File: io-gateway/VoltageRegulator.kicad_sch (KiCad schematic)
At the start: 15 parts, among them U3 TPS54308

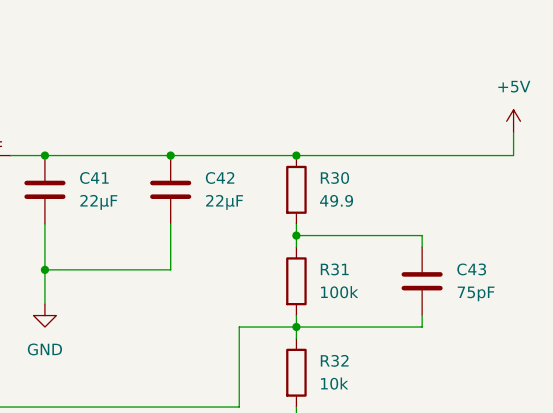
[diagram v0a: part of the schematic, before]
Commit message: increase Pads for Handsolder, fix issue with rectifier
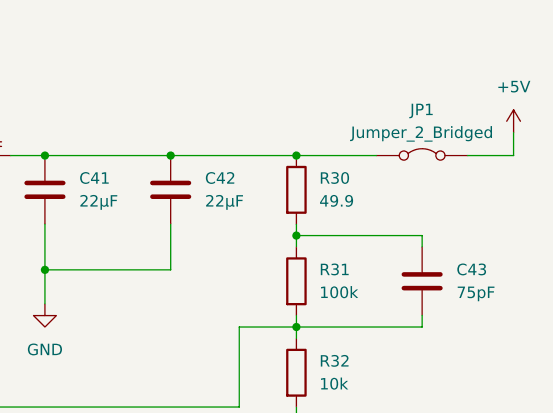
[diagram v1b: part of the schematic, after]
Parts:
- added JP1: Jumper_2_Bridged, Connector_PinHeader_2.54mm:PinHeader_1x02_P2.54mm_Vertical, symbol Jumpers:Jumper_2_Bridged
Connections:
- net +5V: now also JP1.2 (B); no longer C41.1, C42.1, L6.2, R30.1
- new net: C41.1, C42.1, JP1.1 (A), L6.2, R30.1
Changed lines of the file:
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@@
+	)
+	(junction
+		(at 175.26 60.96)
+		(diameter 0)
+		(color 0 0 0 0)
 	)
 	(junction
@@
 	)
 	(junction
-		(at 175.26 60.96)
-		(diameter 0)
-		(color 0 0 0 0)
-	)
-	(junction
 		(at 55.88 58.42)
 		(diameter 0)
@@
 	(wire
 		(pts
+			(xy 175.26 60.96) (xy 184.15 60.96)
+		)
+		(stroke
+			(width 0)
+			(type default)
+		)
+	)
+	(wire
+		(pts
 			(xy 189.23 71.12) (xy 189.23 69.85)
 		)
@@
 	(wire
 		(pts
+			(xy 194.31 60.96) (xy 199.39 60.96)
+		)
+		(stroke
+			(width 0)
+			(type default)
+		)
+	)
+	(wire
+		(pts
 			(xy 175.26 69.85) (xy 175.26 71.12)
 		)
@@
 		(pts
 			(xy 161.29 68.58) (xy 161.29 73.66)
-		)
-		(stroke
-			(width 0)
-			(type default)
-		)
-	)
-	(wire
-		(pts
-			(xy 199.39 60.96) (xy 175.26 60.96)
 		)
 		(stroke
@@
 					(unit 1)
 				)
+			)
+		)
+	)
+	(symbol
+		(lib_id "Jumpers:Jumper_2_Bridged")
+		(at 189.23 60.96 0)
+		(unit 1)
+		(exclude_from_sim no)
+		(in_bom yes)
+		(on_board yes)
+		(dnp no)
+		(fields_autoplaced yes)
+		(property "Reference" "JP1"
+			(at 189.23 55.88 0)
+			(effects
+				(font
+					(size 1.27 1.27)
+				)
+			)
+		)
+		(property "Value" "Jumper_2_Bridged"
+			(at 189.23 58.42 0)
+			(effects
+				(font
+					(size 1.27 1.27)
+				)
+			)
+		)
+		(property "Footprint" "Connector_PinHeader_2.54mm:PinHeader_1x02_P2.54mm_Vertical"
+			(at 189.23 60.96 0)
+			(effects
+				(font
+					(size 1.27 1.27)
+				)
+				(hide yes)
+			)
+		)
+		(property "Datasheet" "~"
+			(at 189.23 60.96 0)
+			(effects
+				(font
+					(size 1.27 1.27)
+				)
+				(hide yes)
+			)
+		)
+		(property "Description" "Jumper, 2-pole, closed/bridged"
+			(at 189.23 60.96 0)
+			(effects
+				(font
+					(size 1.27 1.27)
+				)
+				(hide yes)
+			)
+		)
+		(pin "1"
+		)
+		(pin "2"
+		)
+		(instances
+			(project ""
+				(path "/2cb6f94b-272a-4ed7-b08d-c3630bda6156/9de6c1f0-1e62-4b31-9c57-680b63c27868"
+					(reference "JP1")
+					(unit 1)
+				)

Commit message: V1.2
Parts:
- L6: value 10µF -> 10µH
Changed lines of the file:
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@@
 			)
 		)
-		(property "Value" "10µF"
+		(property "Value" "10µH"
 			(at 139.7 57.15 90)
 			(effects
